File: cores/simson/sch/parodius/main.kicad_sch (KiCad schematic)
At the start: 23 parts

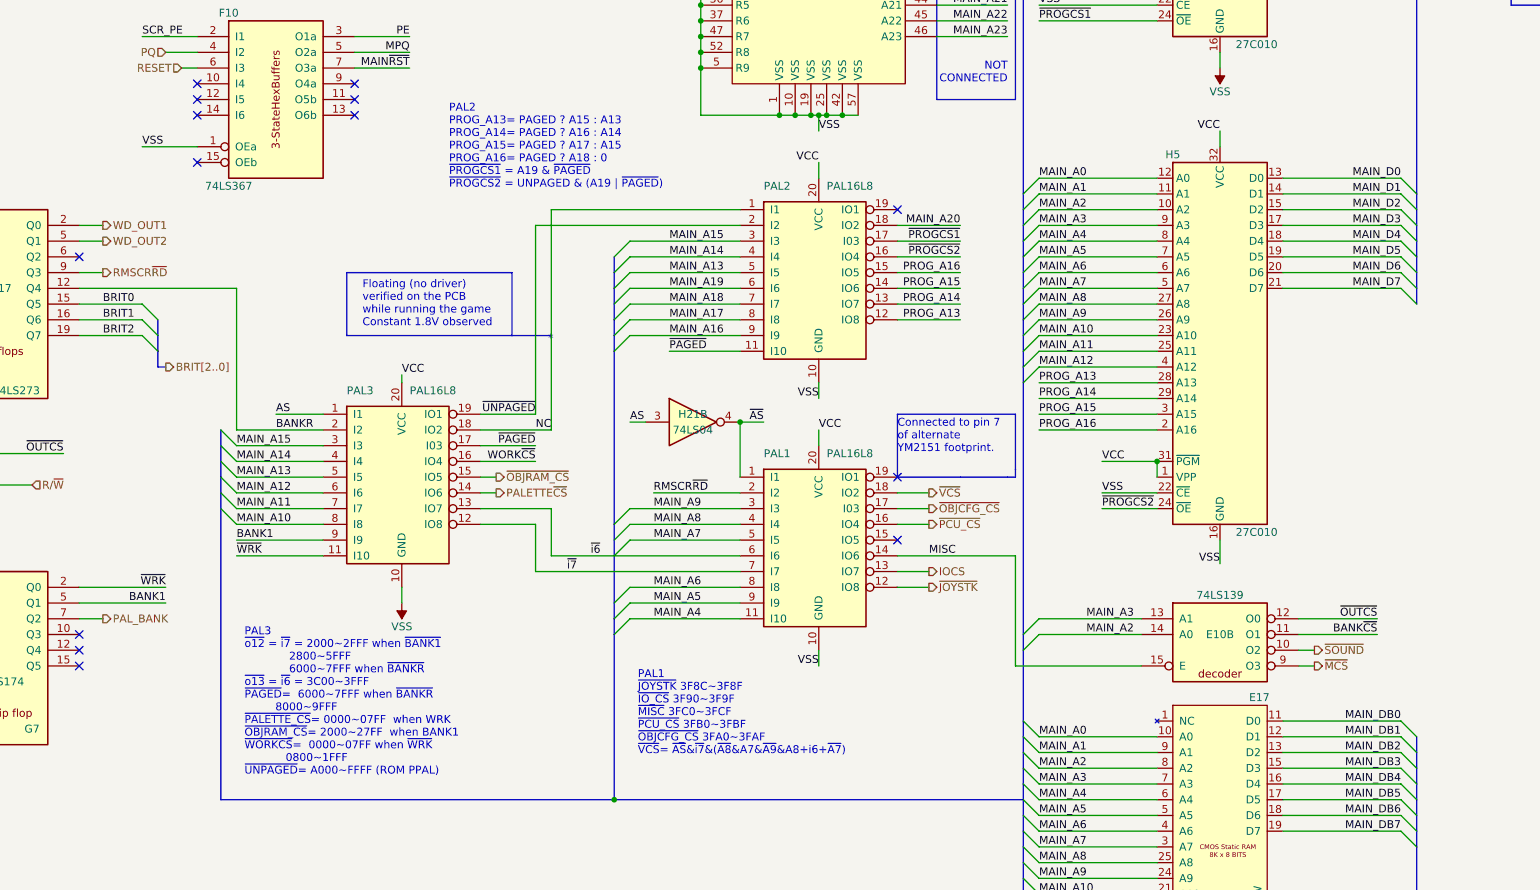
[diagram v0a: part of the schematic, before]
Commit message: simson: Parodius da! boots up
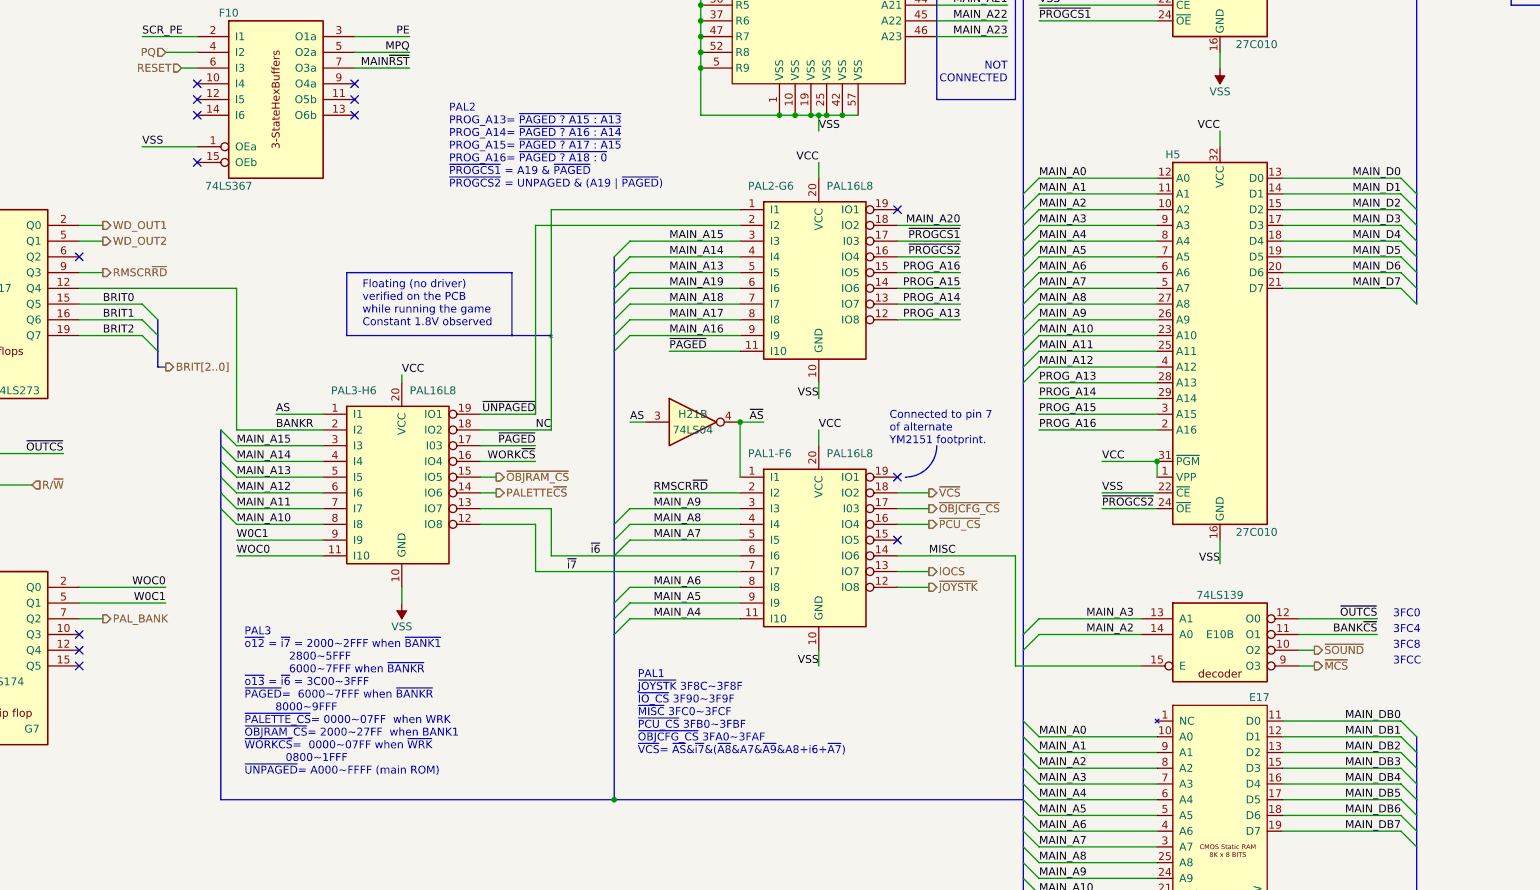
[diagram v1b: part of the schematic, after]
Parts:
- renumbered PAL1 to PAL1-F6, PAL2 to PAL2-G6, PAL3 to PAL3-H6
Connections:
- net BANK1 renamed W0C1
- net ~{WRK} renamed WOC0
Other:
- note added: "3FC0"
- note added: "3FC4"
- note added: "3FC8"
- note added: "3FCC"
- note added: "PAL2 PROG_A13= ~{PAGED ? A15 : A13} PROG_A14= ~{PAGED ? A16 : A14} PROG_A15= ~{PAGED ? A17 : A15} PROG_A16= ~{PAGED ? A18 : 0} ~{PROGCS1} = A19 & ~{PAGED} ~{PROGCS2} = UNPAGED & (A19 | ~{PAGED})"
- note added: "PAL3 ~{o12} = ~{i7} = 2000~2FFF when ~{BANK1} 2800~5FFF 6000~7FFF when ~{BANKR} ~{o13} = ~{i6} = 3C00~3FFF ~{PAGED}= 6000~7FFF when ~{BANKR} 8000~9FFF ~{PALETTE_CS}= 0000~07FF when WRK ~{OBJRAM_CS}= 2000~27FF when BANK1 ~{WORKCS}= 0000~07FF when ~{WRK} 0800~1FFF ~{UNPAGED}= A000~FFFF (main ROM)"
- note removed: "PAL2 PROG_A13= PAGED ? A15 : A13 PROG_A14= PAGED ? A16 : A14 PROG_A15= PAGED ? A17 : A15 PROG_A16= PAGED ? A18 : 0 ~{PROGCS1} = A19 & ~{PAGED} ~{PROGCS2} = UNPAGED & (A19 | ~{PAGED})"
- note removed: "PAL3 ~{o12} = ~{i7} = 2000~2FFF when ~{BANK1} 2800~5FFF 6000~7FFF when ~{BANKR} ~{o13} = ~{i6} = 3C00~3FFF ~{PAGED}= 6000~7FFF when ~{BANKR} 8000~9FFF ~{PALETTE_CS}= 0000~07FF when WRK ~{OBJRAM_CS}= 2000~27FF when BANK1 ~{WORKCS}= 0000~07FF when ~{WRK} 0800~1FFF ~{UNPAGED}= A000~FFFF (ROM PPAL)"
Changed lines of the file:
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@@
     (stroke (width 0) (type default))
   )
-  (polyline (pts (xy 210.82 189.23) (xy 220.98 189.23))
-    (stroke (width 0) (type default))
-  )
   (wire (pts (xy 273.05 69.85) (xy 292.1 69.85))
     (stroke (width 0) (type default))
@@
     (stroke (width 0) (type default))
   )
-  (polyline (pts (xy 210.82 179.07) (xy 210.82 189.23))
-    (stroke (width 0) (type default))
-  )
   (bus (pts (xy 294.64 80.01) (xy 294.64 77.47))
     (stroke (width 0) (type default))
@@
     (stroke (width 0) (type default))
   )
-  (polyline (pts (xy 229.87 187.96) (xy 229.87 179.07))
-    (stroke (width 0) (type default))
-  )
   (wire (pts (xy 210.82 194.31) (xy 215.9 194.31))
     (stroke (width 0) (type default))
@@
     (stroke (width 0) (type default))
   )
-  (polyline (pts (xy 229.87 189.23) (xy 228.6 189.23))
-    (stroke (width 0) (type default))
-  )
   (bus (pts (xy 231.14 173.99) (xy 231.14 214.63))
     (stroke (width 0) (type default))
@@
     (stroke (width 0) (type default))
   )
-  (polyline (pts (xy 229.87 187.96) (xy 229.87 189.23))
-    (stroke (width 0) (type default))
-  )
   (wire (pts (xy 273.05 233.68) (xy 292.1 233.68))
     (stroke (width 0) (type default))
@@
     (stroke (width 0) (type default))
   )
-  (polyline (pts (xy 220.98 189.23) (xy 228.6 189.23))
-    (stroke (width 0) (type default))
-  )
   (wire (pts (xy 217.17 57.15) (xy 220.98 57.15))
     (stroke (width 0) (type default))
@@
     (stroke (width 0) (type default))
   )
-  (polyline (pts (xy 229.87 179.07) (xy 210.82 179.07))
-    (stroke (width 0) (type default))
-  )
   (wire (pts (xy 217.17 95.25) (xy 228.6 95.25))
     (stroke (width 0) (type default))
@@
     (stroke (width 0) (type default))
   )
+  (arc (start 217.17 184.15) (mid 215.6821 187.7421) (end 212.09 189.23)
+    (stroke (width 0) (type default))
+    (fill (type none))
+  )
   (image (at 396.24 260.35) (scale 0.373179)
     (data
@@
     (effects (font (size 1.27 1.27)) (justify left bottom))
   )
-  (text "PAL3\n~{o12} = ~{i7} = 2000~2FFF when ~{BANK1}\n	  	   2800~5FFF\n	  	   6000~7FFF when ~{BANKR}\n~{o13} = ~{i6} = 3C00~3FFF\n~{PAGED}=  6000~7FFF when ~{BANKR}\n	 	8000~9FFF\n~{PALETTE_CS}= 0000~07FF  when WRK\n~{OBJRAM_CS}= 2000~27FF  when BANK1\n~{WORKCS}=  0000~07FF when ~{WRK}\n            0800~1FFF\n~{UNPAGED}= A000~FFFF (ROM PPAL)"
+  (text "PAL3\n~{o12} = ~{i7} = 2000~2FFF when ~{BANK1}\n	  	   2800~5FFF\n	  	   6000~7FFF when ~{BANKR}\n~{o13} = ~{i6} = 3C00~3FFF\n~{PAGED}=  6000~7FFF when ~{BANKR}\n	 	8000~9FFF\n~{PALETTE_CS}= 0000~07FF  when WRK\n~{OBJRAM_CS}= 2000~27FF  when BANK1\n~{WORKCS}=  0000~07FF when ~{WRK}\n            0800~1FFF\n~{UNPAGED}= A000~FFFF (main ROM)"
     (at 105.41 237.49 0)
     (effects (font (size 1.27 1.27)) (justify left bottom))
   )
+  (text "3FC8" (at 290.83 217.17 0)
+    (effects (font (size 1.27 1.27)) (justify left bottom))
+  )
+  (text "3FC0" (at 290.83 212.09 0)
+    (effects (font (size 1.27 1.27)) (justify left bottom))
+  )
   (text "NOT \nCONNECTED" (at 228.6 125.73 0)
     (effects (font (size 1.27 1.27)) (justify right bottom))
@@
     (effects (font (size 1.27 1.27)) (justify left bottom))
   )
-  (text "PAL2\nPROG_A13= PAGED ? A15 : A13\nPROG_A14= PAGED ? A16 : A14\nPROG_A15= PAGED ? A17 : A15\nPROG_A16= PAGED ? A18 : 0\n~{PROGCS1} = A19 & ~{PAGED}\n~{PROGCS2} = UNPAGED & (A19 | ~{PAGED})\n\n"
+  (text "3FCC" (at 290.83 219.71 0)
+    (effects (font (size 1.27 1.27)) (justify left bottom))
+  )
+  (text "PAL2\nPROG_A13= ~{PAGED ? A15 : A13}\nPROG_A14= ~{PAGED ? A16 : A14}\nPROG_A15= ~{PAGED ? A17 : A15}\nPROG_A16= ~{PAGED ? A18 : 0}\n~{PROGCS1} = A19 & ~{PAGED}\n~{PROGCS2} = UNPAGED & (A19 | ~{PAGED})\n\n"
     (at 138.43 144.78 0)
     (effects (font (size 1.27 1.27)) (justify left bottom))
   )
+  (text "3FC4" (at 290.83 214.63 0)
+    (effects (font (size 1.27 1.27)) (justify left bottom))
+  )
   (text "PQ" (at 327.66 41.91 90)
     (effects (font (size 1.27 1.27)) (justify right bottom))
   )
   (text "Connected to pin 7\nof alternate \nYM2151 footprint."
-    (at 210.82 185.42 0)
+    (at 209.55 184.15 0)
     (effects (font (size 1.27 1.27)) (justify left bottom))
   )
@@
     (effects (font (size 1.27 1.27)) (justify left bottom))
   )
-  (label "~{WRK}" (at 92.71 207.01 180) (fields_autoplaced)
+  (label "WOC0" (at 92.71 207.01 180) (fields_autoplaced)
     (effects (font (size 1.27 1.27)) (justify right bottom))
   )
@@
     (effects (font (size 1.27 1.27)) (justify left bottom))
   )
-  (label "~{WRK}" (at 104.14 201.93 0) (fields_autoplaced)
+  (label "WOC0" (at 104.14 201.93 0) (fields_autoplaced)
     (effects (font (size 1.27 1.27)) (justify left bottom))
   )
@@
     (effects (font (size 1.27 1.27)) (justify left bottom))
   )
-  (label "BANK1" (at 104.14 199.39 0) (fields_autoplaced)
+  (label "W0C1" (at 104.14 199.39 0) (fields_autoplaced)
     (effects (font (size 1.27 1.27)) (justify left bottom))
   )
@@
     (effects (font (size 1.27 1.27)) (justify left bottom))
   )
-  (label "BANK1" (at 92.71 209.55 180) (fields_autoplaced)
+  (label "W0C1" (at 92.71 209.55 180) (fields_autoplaced)
     (effects (font (size 1.27 1.27)) (justify right bottom))
   )
@@
   (symbol (lib_id "Logic_Programmable:PAL16L8") (at 130.81 191.77 0) (unit 1)
     (in_bom yes) (on_board yes) (dnp no)
-    (property "Reference" "PAL3" (at 121.92 175.26 0)
+    (property "Reference" "PAL3-H6" (at 119.38 175.26 0)
       (effects (font (size 1.27 1.27)) (justify left))
     )
@@
       (project "paroda"
         (path "/0011ec10-82c4-4039-b424-337480f568e8/7d4ab3ba-37fa-4111-bbdb-c99f1a708a52"
-          (reference "PAL3") (unit 1)
+          (reference "PAL3-H6") (unit 1)
         )
       )
@@
   (symbol (lib_id "Logic_Programmable:PAL16L8") (at 198.12 201.93 0) (unit 1)
     (in_bom yes) (on_board yes) (dnp no)
-    (property "Reference" "PAL1" (at 189.23 185.42 0)
+    (property "Reference" "PAL1-F6" (at 186.69 185.42 0)
       (effects (font (size 1.27 1.27)) (justify left))
     )
@@
       (project "paroda"
         (path "/0011ec10-82c4-4039-b424-337480f568e8/7d4ab3ba-37fa-4111-bbdb-c99f1a708a52"
-          (reference "PAL1") (unit 1)
+          (reference "PAL1-F6") (unit 1)
         )
       )
@@
   (symbol (lib_id "Logic_Programmable:PAL16L8") (at 198.12 158.75 0) (unit 1)
     (in_bom yes) (on_board yes) (dnp no)
-    (property "Reference" "PAL2" (at 189.23 142.24 0)
+    (property "Reference" "PAL2-G6" (at 186.69 142.24 0)
       (effects (font (size 1.27 1.27)) (justify left))
     )
@@
       (project "paroda"
         (path "/0011ec10-82c4-4039-b424-337480f568e8/7d4ab3ba-37fa-4111-bbdb-c99f1a708a52"
-          (reference "PAL2") (unit 1)
+          (reference "PAL2-G6") (unit 1)
         )
       )

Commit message: wip #517 paroda
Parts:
- renumbered PAL1-F6 to PAL1, PAL2-G6 to PAL2, PAL3-H6 to PAL3
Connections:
- net AS: now also F19.10 (~{S}), F19.4 (~{S}), H21.4, H22.1 (~{R}), PAL1.1 (I1); no longer F19.12 (D), FP2.20 (Pin_20), H12.16 (AS), H21.3, PAL3.1 (I1)
- net ~{AS}: now also F19.12 (D), FP2.20 (Pin_20), H12.16 (AS), H21.3, PAL3.1 (I1); no longer F19.10 (~{S}), F19.4 (~{S}), H21.4, H22.1 (~{R}), PAL1.1 (I1)
- net BRIT0 renamed MBRIT0
- net BRIT1 renamed MBRIT1
- net BRIT2 renamed MBRIT2
- net MAIN_A0 renamed ~{LDS}
- net MAIN~{DS} renamed ~{MDS}
- net W0C1 renamed BANK1
- net WOC0 renamed ~{WRK}
- net ~{MCS} renamed ~{SOREG}
- net ~{OBJCFG_CS} renamed ~{OBJSET}
- net ~{SOUND} renamed ~{SOON}
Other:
- note added: "PAL1 ~{JOYSTK} 3F8C~3F8F ~{IO_CS} 3F90~3F9F ~{MISC} 3FC0~3FCF ~{PCU_CS} 3FB0~3FBF ~{OBJSET} 3FA0~3FAF ~{VCS}= AS&~{i7}&(~{A8}&A7&~{A9}&A8+i6+~{A7})"
- note added: "PAL2 PROG_A13= PAGED ? A15 : A13 PROG_A14= PAGED ? A16 : A14 PROG_A15= PAGED ? A17 : A15 PROG_A16= PAGED ? A18 : 0 ~{PROGCS1} = A19 & ~{PAGED} ~{PROGCS2} = UNPAGED & (A19 | ~{PAGED})"
- note added: "PAL3 ~{o12} = ~{i7} = 2000~2FFF when ~{BANK1} 2800~5FFF 6000~7FFF when ~{BANKR} ~{o13} = ~{i6} = 3C00~3FFF ~{PAGED}= 6000~7FFF when ~{BANKR} 8000~9FFF ~{PALETTE_CS}= 0000~07FF when WRK ~{OBJRAM_CS}= 2000~27FF when BANK1 ~{WORKCS}= 0000~07FF when ~{WRK} 0800~1FFF ~{UNPAGED}= A000~FFFF (ROM PPAL)"
- note removed: "3FC0"
- note removed: "3FC4"
- note removed: "3FC8"
- note removed: "3FCC"
- note removed: "PAL1 ~{JOYSTK} 3F8C~3F8F ~{IO_CS} 3F90~3F9F ~{MISC} 3FC0~3FCF ~{PCU_CS} 3FB0~3FBF ~{OBJCFG_CS} 3FA0~3FAF ~{VCS}= ~{AS}&~{i7}&(~{A8}&A7&~{A9}&A8+i6+~{A7})"
- note removed: "PAL2 PROG_A13= ~{PAGED ? A15 : A13} PROG_A14= ~{PAGED ? A16 : A14} PROG_A15= ~{PAGED ? A17 : A15} PROG_A16= ~{PAGED ? A18 : 0} ~{PROGCS1} = A19 & ~{PAGED} ~{PROGCS2} = UNPAGED & (A19 | ~{PAGED})"
- note removed: "PAL3 ~{o12} = ~{i7} = 2000~2FFF when ~{BANK1} 2800~5FFF 6000~7FFF when ~{BANKR} ~{o13} = ~{i6} = 3C00~3FFF ~{PAGED}= 6000~7FFF when ~{BANKR} 8000~9FFF ~{PALETTE_CS}= 0000~07FF when WRK ~{OBJRAM_CS}= 2000~27FF when BANK1 ~{WORKCS}= 0000~07FF when ~{WRK} 0800~1FFF ~{UNPAGED}= A000~FFFF (main ROM)"
